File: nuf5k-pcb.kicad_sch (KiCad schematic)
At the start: 209 parts, among them J1 AVR-ISP-6, J2 1734366-1, J3 1734366-1, J4 1734366-1, SW0 KEYSW, SW1 KEYSW, SW10 KEYSW, SW11 KEYSW, SW12 KEYSW, SW13 KEYSW, SW14 KEYSW, SW15 KEYSW, SW16 KEYSW, SW17 KEYSW, SW18 KEYSW, SW19 KEYSW, SW2 KEYSW, SW20 KEYSW, SW21 KEYSW, SW22 KEYSW, SW23 KEYSW, SW24 KEYSW, SW25 KEYSW, SW26 KEYSW, SW27 KEYSW, SW28 KEYSW, SW29 KEYSW, SW3 KEYSW, SW30 KEYSW, SW31 KEYSW, SW32 KEYSW, SW33 KEYSW, SW34 KEYSW, SW35 KEYSW, SW36 KEYSW, SW37 KEYSW, SW38 KEYSW, SW39 KEYSW, SW4 KEYSW, SW40 KEYSW, SW41 KEYSW, SW42 KEYSW, SW43 KEYSW, SW44 KEYSW, SW45 KEYSW, SW46 KEYSW, SW47 KEYSW, SW48 KEYSW, SW49 KEYSW, SW5 KEYSW, SW50 KEYSW, SW51 KEYSW, SW52 KEYSW, SW53 KEYSW, SW54 KEYSW, SW55 KEYSW, SW56 KEYSW, SW57 KEYSW, SW58 KEYSW, SW59 KEYSW, SW6 KEYSW, SW60 KEYSW, SW61 KEYSW, SW62 KEYSW, SW63 KEYSW, SW64 KEYSW, SW65 KEYSW, SW66 KEYSW, SW67 KEYSW, SW68 KEYSW, SW69 KEYSW, SW7 KEYSW, SW70 KEYSW, SW71 KEYSW, SW72 KEYSW, SW73 KEYSW, SW74 KEYSW, SW75 KEYSW, SW76 KEYSW, SW77 KEYSW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

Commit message: FE1.1s works
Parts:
- added C10, C11, C9: 100u, Capacitor_SMD:C_0201_0603Metric, symbol Device:C
- added C6, C8: 10u, Capacitor_SMD:C_0201_0603Metric, symbol Device:C
- added C7: 1u, Capacitor_SMD:C_0201_0603Metric, symbol Device:C
- added R9: 2k7, symbol Device:R
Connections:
- net +5V: now also U2.20 (VDD5), C10.2, C11.2, C7.2, C8.2, C9.2
- net GND: now also C10.1, C11.1, C6.2, C7.1, C8.1, C9.1, R9.2
- net at U2.13 (VD33): now also U2.17 (~{XRSTJ}), U2.21 (VD33_O), C6.1
- net at U2.14 (REXT): now also R9.1
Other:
- note added: "https://circuitneato.com/media/2025/06/USB-Hub-FE1.1S-Ports.pdf"
- note removed: "https://electronics.stackexchange.com/questions/350140/how-can-i-add-additional-components-and-connections-to-make-this-usb-hub-functio"
- moved on the sheet: C1, C2, J2, J3, J4, U2, Y1

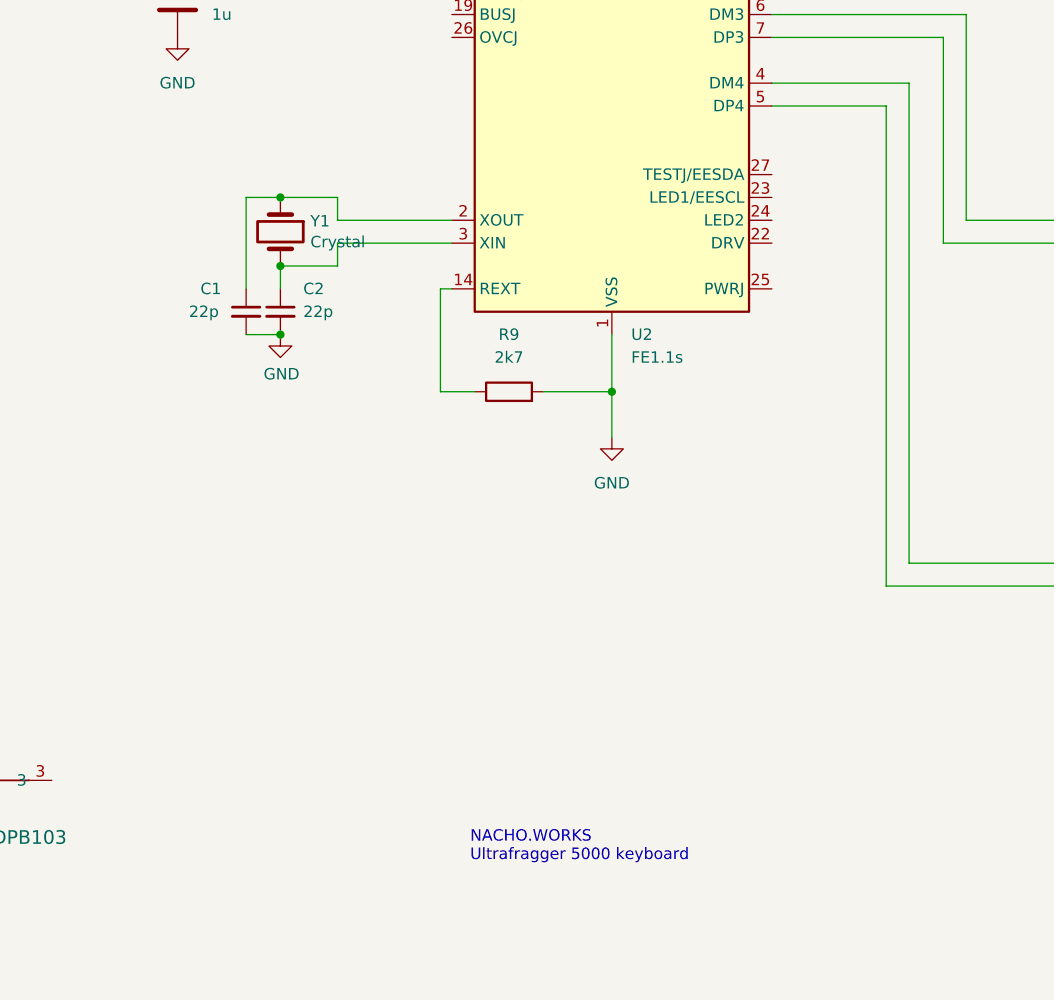
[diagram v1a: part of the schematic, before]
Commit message: FE1.1s added EEPROM
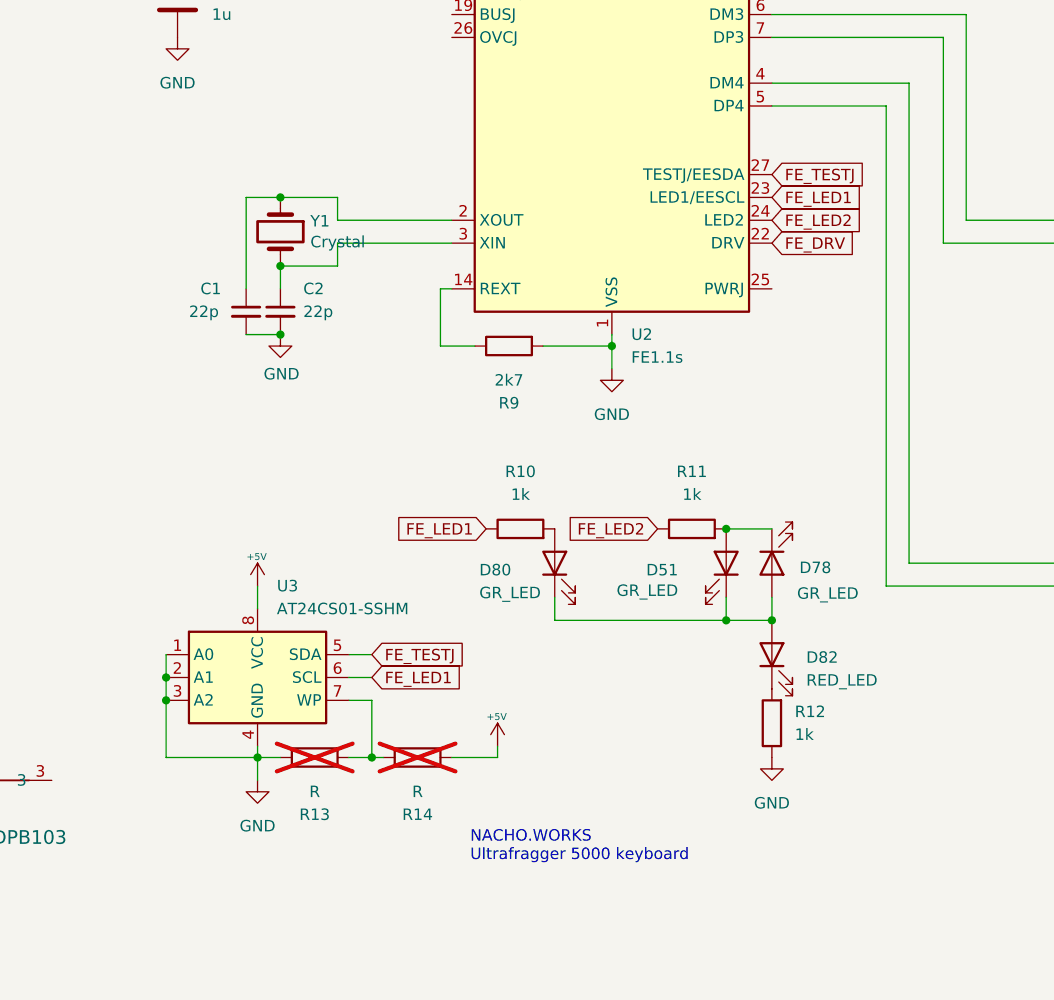
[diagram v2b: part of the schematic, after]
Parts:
- added D51, D78, D80: GR_LED, LED_SMD:LED_0402_1005Metric, symbol Device:LED
- added D82: RED_LED, LED_SMD:LED_0402_1005Metric, symbol Device:LED
- added R10, R11, R12: 1k, symbol Device:R
- added R13, R14: R, Resistor_SMD:R_0402_1005Metric, symbol Device:R
- added U3: AT24CS01-SSHM, Package_SO:SOIC-8_3.9x4.9mm_P1.27mm, symbol Memory_EEPROM:AT24CS01-SSHM
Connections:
- net +5V: now also R14.2, U3.8 (VCC)
- net GND: now also R12.1, R13.1, U3.1 (A0), U3.2 (A1), U3.3 (A2), U3.4 (GND)
- net FE_DRV: now reaches U2.22 (DRV)
- net FE_LED1: now reaches U2.23 (LED1/EESCL)
- net FE_LED1: now also R10.1, U3.6 (SCL)
- net FE_LED2: now reaches U2.24 (LED2)
- net FE_LED2: now also R11.1
- net FE_TESTJ: now reaches U2.27 (TESTJ/EESDA)
- net FE_TESTJ: now also U3.5 (SDA)
- new net: R13.2, R14.1, U3.7 (WP)
- new net: D51.2 (A), D78.1 (K), R11.2
- new net: D82.1 (K), R12.2
- new net: D80.2 (A), R10.2
- new net: D51.1 (K), D78.2 (A), D80.1 (K), D82.2 (A)
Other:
- moved on the sheet: R9
